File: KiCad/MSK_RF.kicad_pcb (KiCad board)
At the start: 2 copper layers, 52 x 73.5 mm, 65 parts, among them J1 Conn_01x05_Male, J2 Conn_01x12, J3 Conn_01x12, J4 Conn_Coaxial, J5 47346-0001, U1 STM32WLE5CCU6, U2 ADG918BRM, U3 TLV70233_SOT23-5, Y1 32.768 kHz, Y2 ECS-320-8-37-CKM-TR3

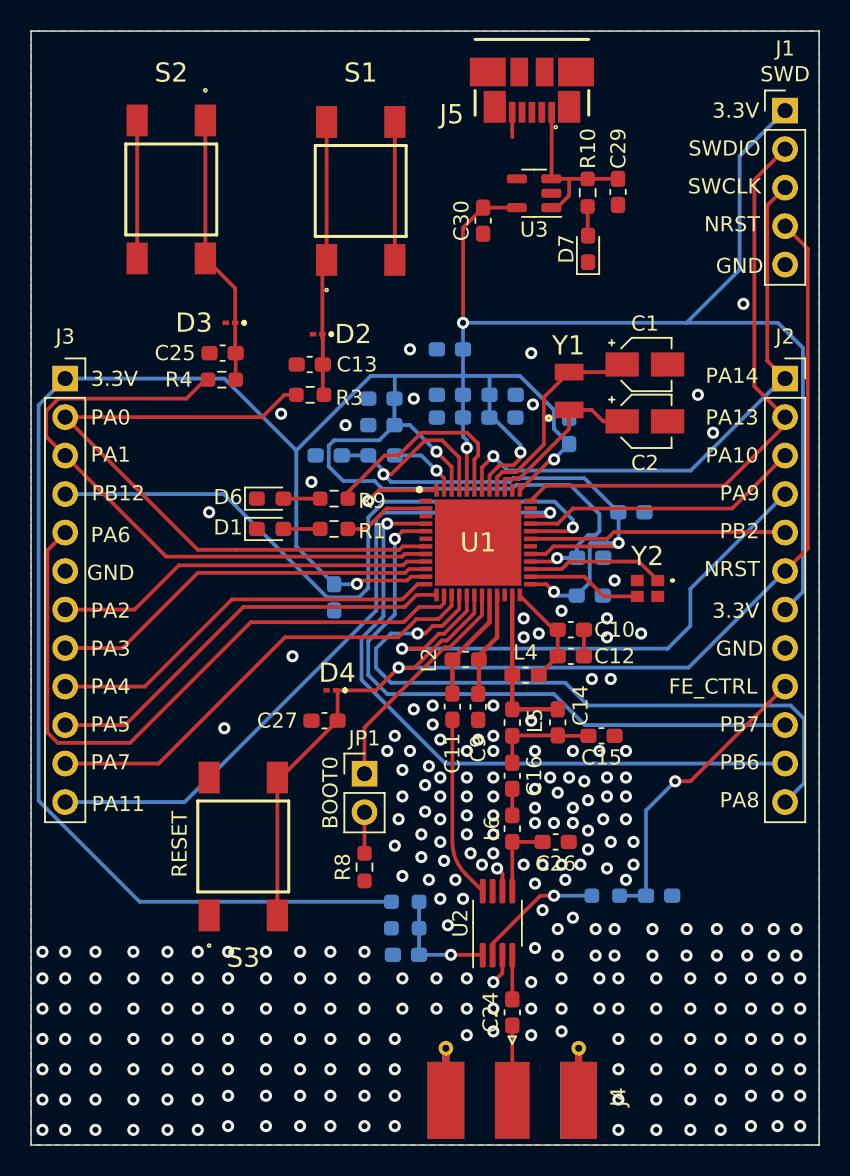
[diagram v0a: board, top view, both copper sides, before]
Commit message: drc inspection solved
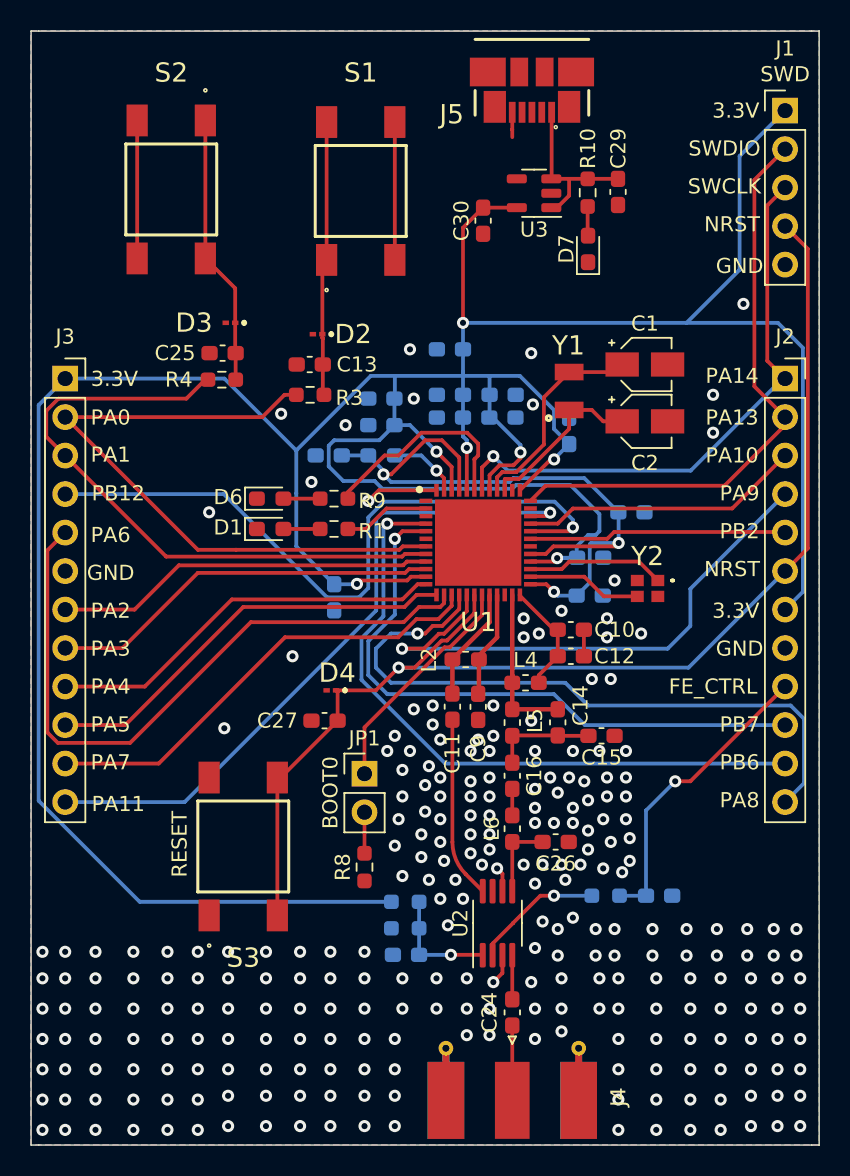
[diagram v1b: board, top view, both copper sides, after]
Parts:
- moved L4 0.50 mm to (70.1, 115.2)
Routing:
- net Net-(C10-Pad2): track 7.00 -> 7.50 mm
- net GND: vias 264 -> 265
- net (no net): vias 1 -> 0
